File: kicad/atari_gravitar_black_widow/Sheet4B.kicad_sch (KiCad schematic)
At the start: 45 parts

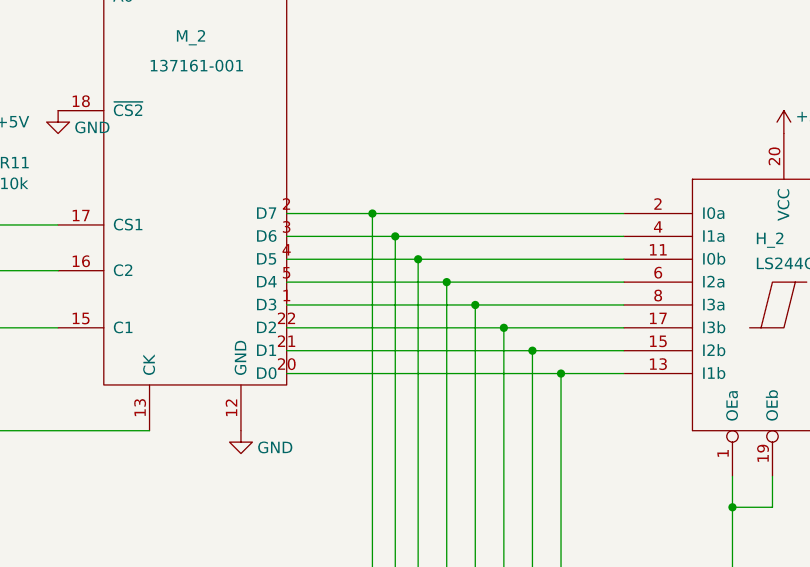
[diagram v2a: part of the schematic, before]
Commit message: Fixed all warnings and errors
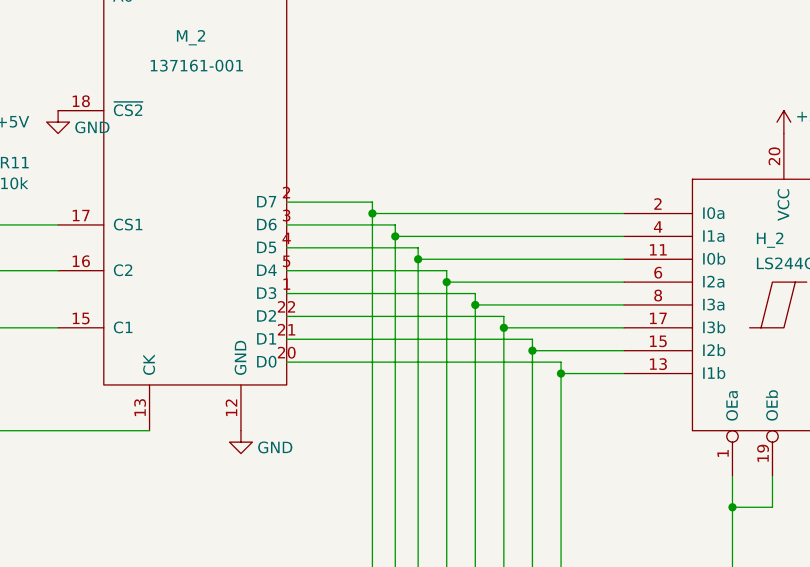
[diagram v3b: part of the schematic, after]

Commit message: place ttl
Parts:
- A_4: footprint (none) -> Star_Wars_Vector_PCB:DIP8
- B_6: footprint (none) -> Star_Wars_Vector_PCB:DIP14
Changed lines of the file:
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@@
     (property "Reference" "B_6" (id 0) (at 102.235 271.7505 0))
     (property "Value" "S86" (id 1) (at 102.235 274.5256 0))
-    (property "Footprint" "" (id 2) (at 102.235 280.67 0)
+    (property "Footprint" "Star_Wars_Vector_PCB:DIP14" (id 2) (at 102.235 280.67 0)
       (effects (font (size 1.27 1.27)) hide)
     )
@@
     (property "Reference" "A_4" (id 0) (at 372.11 104.14 0))
     (property "Value" "555" (id 1) (at 372.11 106.68 0))
-    (property "Footprint" "" (id 2) (at 372.11 104.775 0)
-      (effects (font (size 1.27 1.27)) hide)
-    )
+    (property "Footprint" "Star_Wars_Vector_PCB:DIP8" (id 2) (at 372.11 104.775 0)
+      (effects (font (size 1.27 1.27)) hide)
+    )

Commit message: more ttl placements
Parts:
- D_1, E/F_1, H_1: footprint (none) -> Star_Wars_Vector_PCB:DDIP24
- E_2, H_2: footprint (none) -> Star_Wars_Vector_PCB:DIP20
- E_3: footprint (none) -> Star_Wars_Vector_PCB:DIP14
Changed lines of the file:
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@@
     (property "Reference" "E_3" (id 0) (at 195.961 185.6929 0))
     (property "Value" "LS00" (id 1) (at 195.961 188.468 0))
-    (property "Footprint" "" (id 2) (at 196.85 187.96 0)
+    (property "Footprint" "Star_Wars_Vector_PCB:DIP14" (id 2) (at 196.85 187.96 0)
       (effects (font (size 1.27 1.27)) hide)
     )
@@
       (effects (font (size 1.27 1.27)) (justify left))
     )
-    (property "Footprint" "" (id 2) (at 506.73 198.12 0)
+    (property "Footprint" "Star_Wars_Vector_PCB:DIP20" (id 2) (at 506.73 198.12 0)
       (effects (font (size 1.27 1.27)) hide)
     )
@@
       (effects (font (size 1.27 1.27)) (justify left))
     )
-    (property "Footprint" "" (id 2) (at 219.71 127 0)
+    (property "Footprint" "Star_Wars_Vector_PCB:DIP20" (id 2) (at 219.71 127 0)
       (effects (font (size 1.27 1.27)) hide)
     )
@@
       (effects (font (size 1.27 1.27)) (justify right))
     )
-    (property "Footprint" "" (id 2) (at 172.085 96.52 0)
+    (property "Footprint" "Star_Wars_Vector_PCB:DDIP24" (id 2) (at 172.085 96.52 0)
       (effects (font (size 1.27 1.27)) hide)
     )
@@
       (effects (font (size 1.27 1.27)) (justify right))
     )
-    (property "Footprint" "" (id 2) (at 131.445 96.52 0)
+    (property "Footprint" "Star_Wars_Vector_PCB:DDIP24" (id 2) (at 131.445 96.52 0)
       (effects (font (size 1.27 1.27)) hide)
     )
@@
       (effects (font (size 1.27 1.27)) (justify right))
     )
-    (property "Footprint" "" (id 2) (at 151.765 96.52 0)
-      (effects (font (size 1.27 1.27)) hide)
-    )
+    (property "Footprint" "Star_Wars_Vector_PCB:DDIP24" (id 2) (at 151.765 96.52 0)
+      (effects (font (size 1.27 1.27)) hide)
+    )

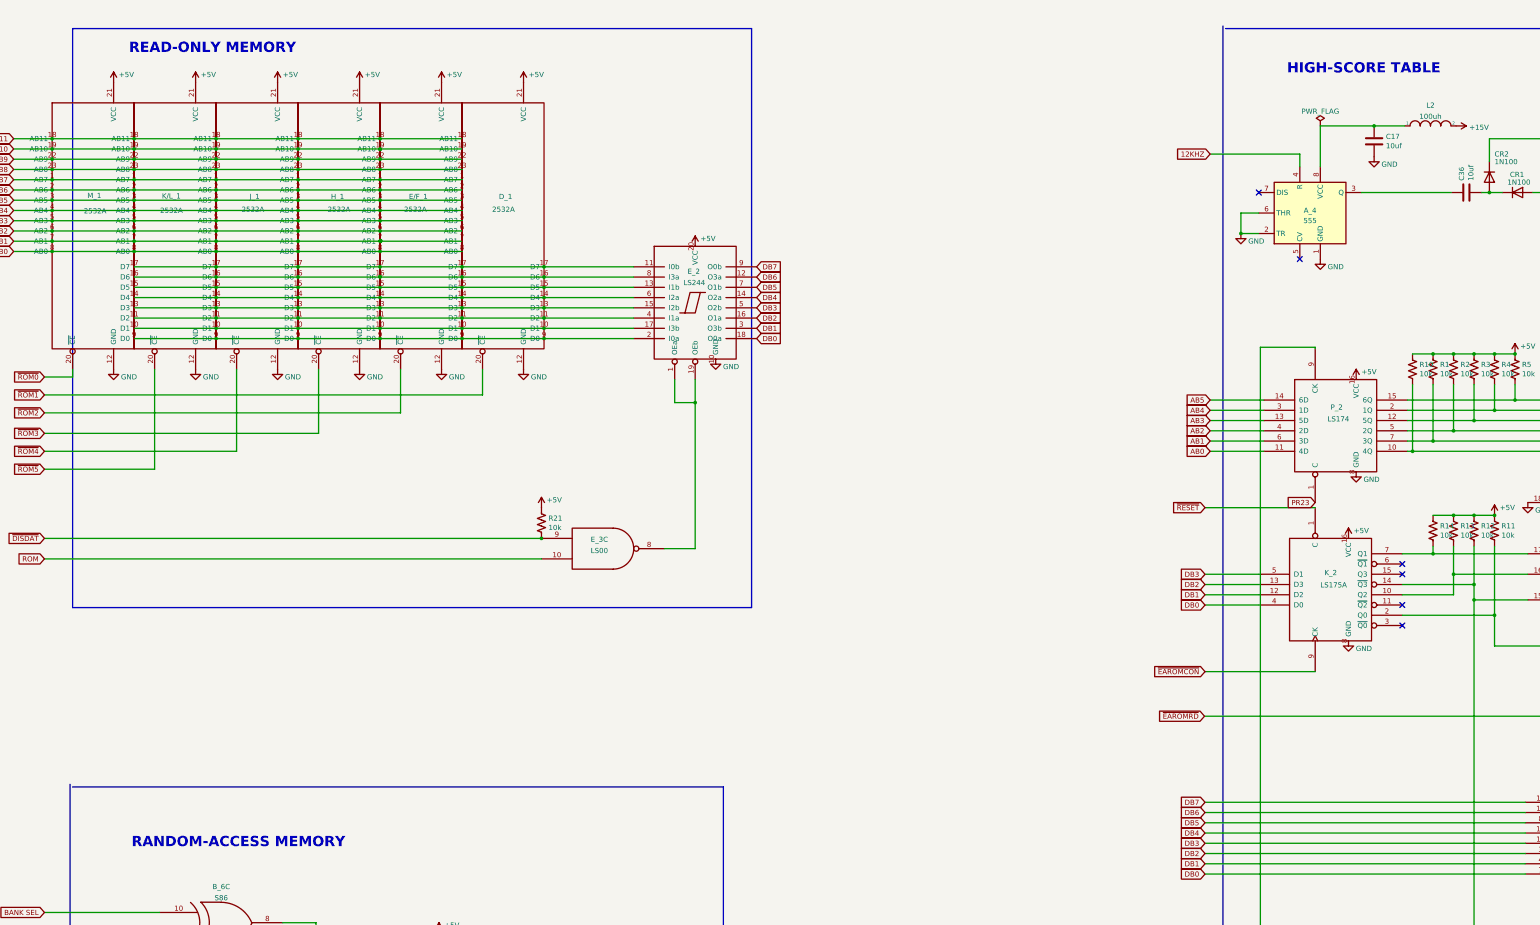
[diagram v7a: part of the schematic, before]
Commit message: some routing and E2 bus fix
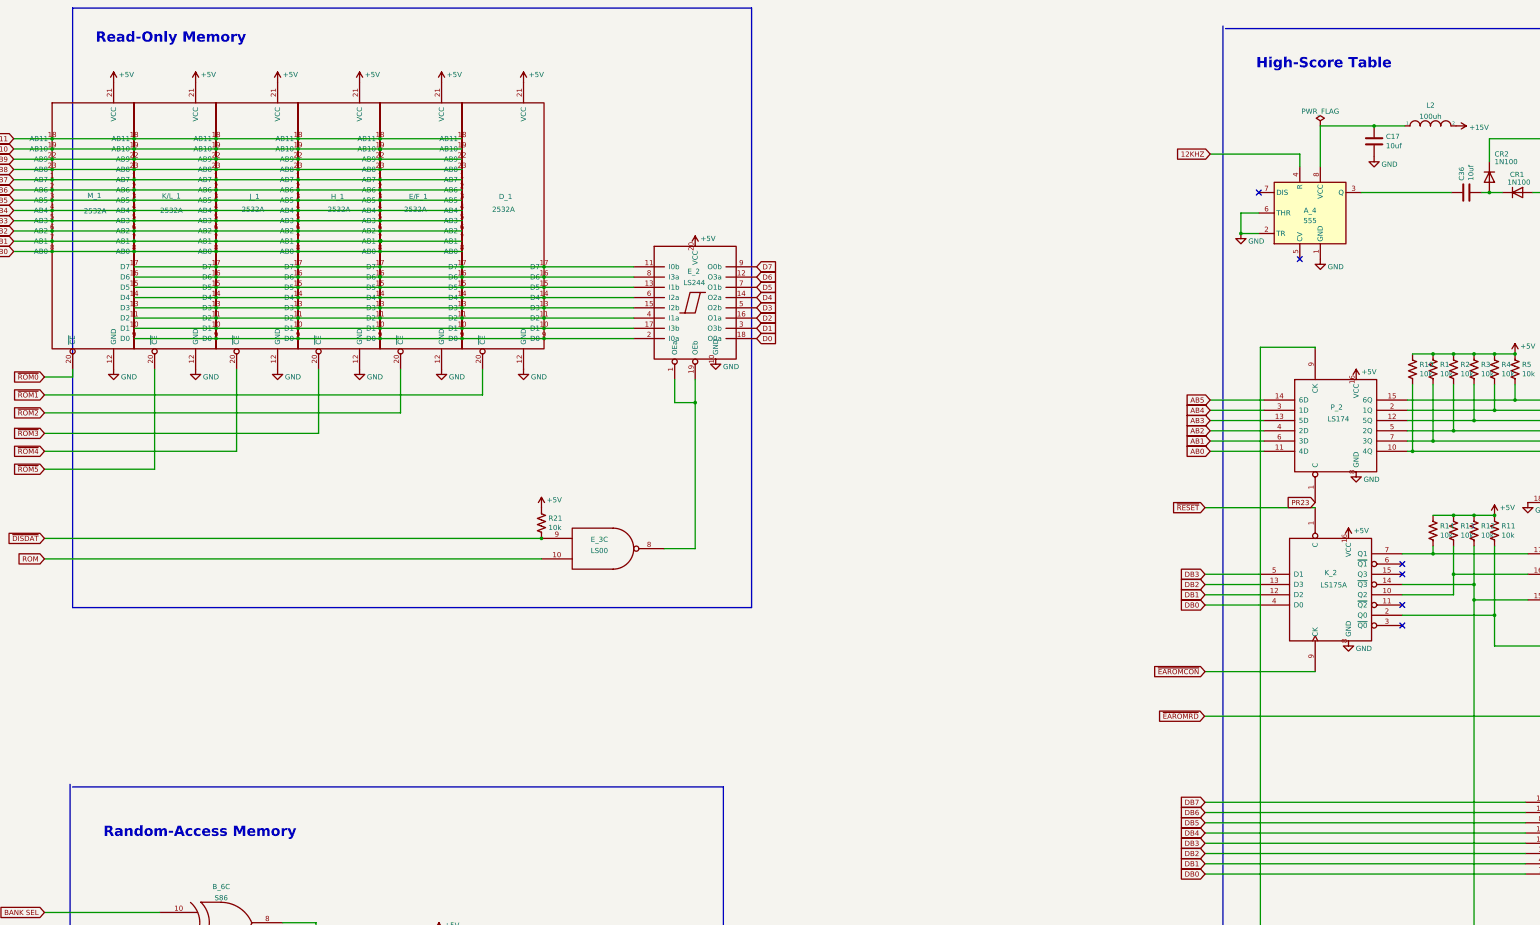
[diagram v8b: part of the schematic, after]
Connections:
- net DB0: no longer E_2.18 (O0a)
- net DB1: no longer E_2.3 (O3b)
- net DB2: no longer E_2.16 (O1a)
- net DB3: no longer E_2.5 (O2b)
- net DB4: no longer E_2.14 (O2a)
- net DB5: no longer E_2.7 (O1b)
- net DB6: no longer E_2.12 (O3a)
- net DB7: no longer E_2.9 (O0b)
- new net D0: E_2.18 (O0a)
- new net D1: E_2.3 (O3b)
- new net D2: E_2.16 (O1a)
- new net D3: E_2.5 (O2b)
- new net D4: E_2.14 (O2a)
- new net D5: E_2.7 (O1b)
- new net D6: E_2.12 (O3a)
- new net D7: E_2.9 (O0b)
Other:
- note added: "High-Score Table"
- note added: "Random-Access Memory"
- note added: "Read-Only Memory"
- note removed: "HIGH-SCORE TABLE"
- note removed: "RANDOM-ACCESS MEMORY"
- note removed: "READ-ONLY MEMORY"
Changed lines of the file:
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@@
     (stroke (width 0) (type default) (color 0 0 0 0))
   )
-  (polyline (pts (xy 65.405 59.055) (xy 65.405 202.565))
+  (polyline (pts (xy 65.405 53.975) (xy 65.405 202.565))
     (stroke (width 0) (type default) (color 0 0 0 0))
   )
@@
     (stroke (width 0) (type default) (color 0 0 0 0))
   )
-  (polyline (pts (xy 233.68 59.055) (xy 233.68 202.565))
+  (polyline (pts (xy 233.68 53.975) (xy 233.68 202.565))
     (stroke (width 0) (type default) (color 0 0 0 0))
   )
@@
     (stroke (width 0) (type default) (color 0 0 0 0))
   )
-  (polyline (pts (xy 65.405 59.055) (xy 233.68 59.055))
+  (polyline (pts (xy 65.405 53.975) (xy 233.68 53.975))
     (stroke (width 0) (type default) (color 0 0 0 0))
   )
@@
     (stroke (width 0) (type default) (color 0 0 0 0))
   )
-  (text "READ-ONLY MEMORY\n" (at 79.375 65.405 0)
+  (text "Read-Only Memory" (at 71.12 62.865 0)
     (effects (font (size 2.54 2.54) (thickness 0.508) bold) (justify left bottom))
   )
-  (text "RANDOM-ACCESS MEMORY\n" (at 80.01 262.255 0)
+  (text "Random-Access Memory" (at 73.025 259.715 0)
     (effects (font (size 2.54 2.54) (thickness 0.508) bold) (justify left bottom))
   )
-  (text "HIGH-SCORE TABLE\n" (at 366.395 70.485 0)
+  (text "High-Score Table" (at 358.775 69.215 0)
     (effects (font (size 2.54 2.54) (thickness 0.508) bold) (justify left bottom))
   )
@@
     )
   )
-  (global_label "DB5" (shape input) (at 234.95 123.19 0) (fields_autoplaced)
-    (effects (font (size 1.27 1.27)) (justify left))
-    (property "Intersheet References" "${INTERSHEET_REFS}" (id 0) (at 241.0237 123.1106 0)
+  (global_label "D5" (shape input) (at 234.95 123.19 0) (fields_autoplaced)
+    (effects (font (size 1.27 1.27)) (justify left))
+    (property "Intersheet References" "${INTERSHEET_REFS}" (id 0) (at 239.7537 123.1106 0)
       (effects (font (size 1.27 1.27)) (justify left) hide)
     )
@@
     )
   )
-  (global_label "DB7" (shape input) (at 234.95 118.11 0) (fields_autoplaced)
-    (effects (font (size 1.27 1.27)) (justify left))
-    (property "Intersheet References" "${INTERSHEET_REFS}" (id 0) (at 241.0237 118.0306 0)
+  (global_label "D7" (shape input) (at 234.95 118.11 0) (fields_autoplaced)
+    (effects (font (size 1.27 1.27)) (justify left))
+    (property "Intersheet References" "${INTERSHEET_REFS}" (id 0) (at 239.7537 118.0306 0)
       (effects (font (size 1.27 1.27)) (justify left) hide)
     )
@@
     )
   )
-  (global_label "DB6" (shape input) (at 234.95 120.65 0) (fields_autoplaced)
-    (effects (font (size 1.27 1.27)) (justify left))
-    (property "Intersheet References" "${INTERSHEET_REFS}" (id 0) (at 241.0237 120.5706 0)
+  (global_label "D6" (shape input) (at 234.95 120.65 0) (fields_autoplaced)
+    (effects (font (size 1.27 1.27)) (justify left))
+    (property "Intersheet References" "${INTERSHEET_REFS}" (id 0) (at 239.7537 120.5706 0)
       (effects (font (size 1.27 1.27)) (justify left) hide)
     )
@@
     )
   )
-  (global_label "DB3" (shape input) (at 234.95 128.27 0) (fields_autoplaced)
-    (effects (font (size 1.27 1.27)) (justify left))
-    (property "Intersheet References" "${INTERSHEET_REFS}" (id 0) (at 241.0237 128.1906 0)
-      (effects (font (size 1.27 1.27)) (justify left) hide)
-    )
-  )
-  (global_label "DB1" (shape input) (at 234.95 133.35 0) (fields_autoplaced)
-    (effects (font (size 1.27 1.27)) (justify left))
-    (property "Intersheet References" "${INTERSHEET_REFS}" (id 0) (at 241.0237 133.2706 0)
+  (global_label "D3" (shape input) (at 234.95 128.27 0) (fields_autoplaced)
+    (effects (font (size 1.27 1.27)) (justify left))
+    (property "Intersheet References" "${INTERSHEET_REFS}" (id 0) (at 239.7537 128.1906 0)
+      (effects (font (size 1.27 1.27)) (justify left) hide)
+    )
+  )
+  (global_label "D1" (shape input) (at 234.95 133.35 0) (fields_autoplaced)
+    (effects (font (size 1.27 1.27)) (justify left))
+    (property "Intersheet References" "${INTERSHEET_REFS}" (id 0) (at 239.7537 133.2706 0)
       (effects (font (size 1.27 1.27)) (justify left) hide)
     )
@@
     )
   )
-  (global_label "DB0" (shape input) (at 234.95 135.89 0) (fields_autoplaced)
-    (effects (font (size 1.27 1.27)) (justify left))
-    (property "Intersheet References" "${INTERSHEET_REFS}" (id 0) (at 241.0237 135.8106 0)
-      (effects (font (size 1.27 1.27)) (justify left) hide)
-    )
-  )
-  (global_label "DB4" (shape input) (at 234.95 125.73 0) (fields_autoplaced)
-    (effects (font (size 1.27 1.27)) (justify left))
-    (property "Intersheet References" "${INTERSHEET_REFS}" (id 0) (at 241.0237 125.6506 0)
-      (effects (font (size 1.27 1.27)) (justify left) hide)
-    )
-  )
-  (global_label "DB2" (shape input) (at 234.95 130.81 0) (fields_autoplaced)
-    (effects (font (size 1.27 1.27)) (justify left))
-    (property "Intersheet References" "${INTERSHEET_REFS}" (id 0) (at 241.0237 130.7306 0)
-      (effects (font (size 1.27 1.27)) (justify left) hide)
-    )
+  (global_label "D0" (shape input) (at 234.95 135.89 0) (fields_autoplaced)
+    (effects (font (size 1.27 1.27)) (justify left))
+    (property "Intersheet References" "${INTERSHEET_REFS}" (id 0) (at 239.7537 135.8106 0)
+      (effects (font (size 1.27 1.27)) (justify left) hide)
+    )
+  )
+  (global_label "D4" (shape input) (at 234.95 125.73 0) (fields_autoplaced)
+    (effects (font (size 1.27 1.27)) (justify left))
+    (property "Intersheet References" "${INTERSHEET_REFS}" (id 0) (at 239.7537 125.6506 0)
+      (effects (font (size 1.27 1.27)) (justify left) hide)
+    )
+  )
+  (global_label "D2" (shape input) (at 234.95 130.81 0) (fields_autoplaced)
+    (effects (font (size 1.27 1.27)) (justify left))
+    (property "Intersheet References" "${INTERSHEET_REFS}" (id 0) (at 239.7537 130.7306 0)
+      (effects (font (size 1.27 1.27)) (justify left) hide)
+    )
